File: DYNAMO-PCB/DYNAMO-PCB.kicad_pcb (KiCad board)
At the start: 2 copper layers, 43 parts, among them J1 HDMI_A, J10 Conn_01x03_Pin, J11 Conn_01x03_Pin, J12 Conn_01x03_Pin, J13 Conn_01x02_Pin, J17 USB3_A, J18 USB3_A, J19 USB3_A, J2 USB3_A, J20 USB3_A, J21 USB3_A, J22 USB3_A, J23 USB3_A, J24 USB3_A, J25 USB3_A, J26 USB_C_Receptacle_USB2.0_16P, J27 USB_C_Receptacle_USB2.0_16P, J28 USB_C_Receptacle_USB2.0_16P, J29 USB_C_Receptacle_USB2.0_16P, J3 Conn_01x03_Pin, J30 USB_C_Receptacle_USB2.0_16P, J31 USB3_A, J32 USB3_A, J33 Conn_02x05_Counter_Clockwise, J34 Conn_02x05_Counter_Clockwise, J5 Conn_01x02_Pin, J6 Conn_01x03_Pin, J7 Conn_01x08_Socket, J8 Conn_01x03_Pin, J9 Conn_01x03_Pin, U2 CH7035B-BF

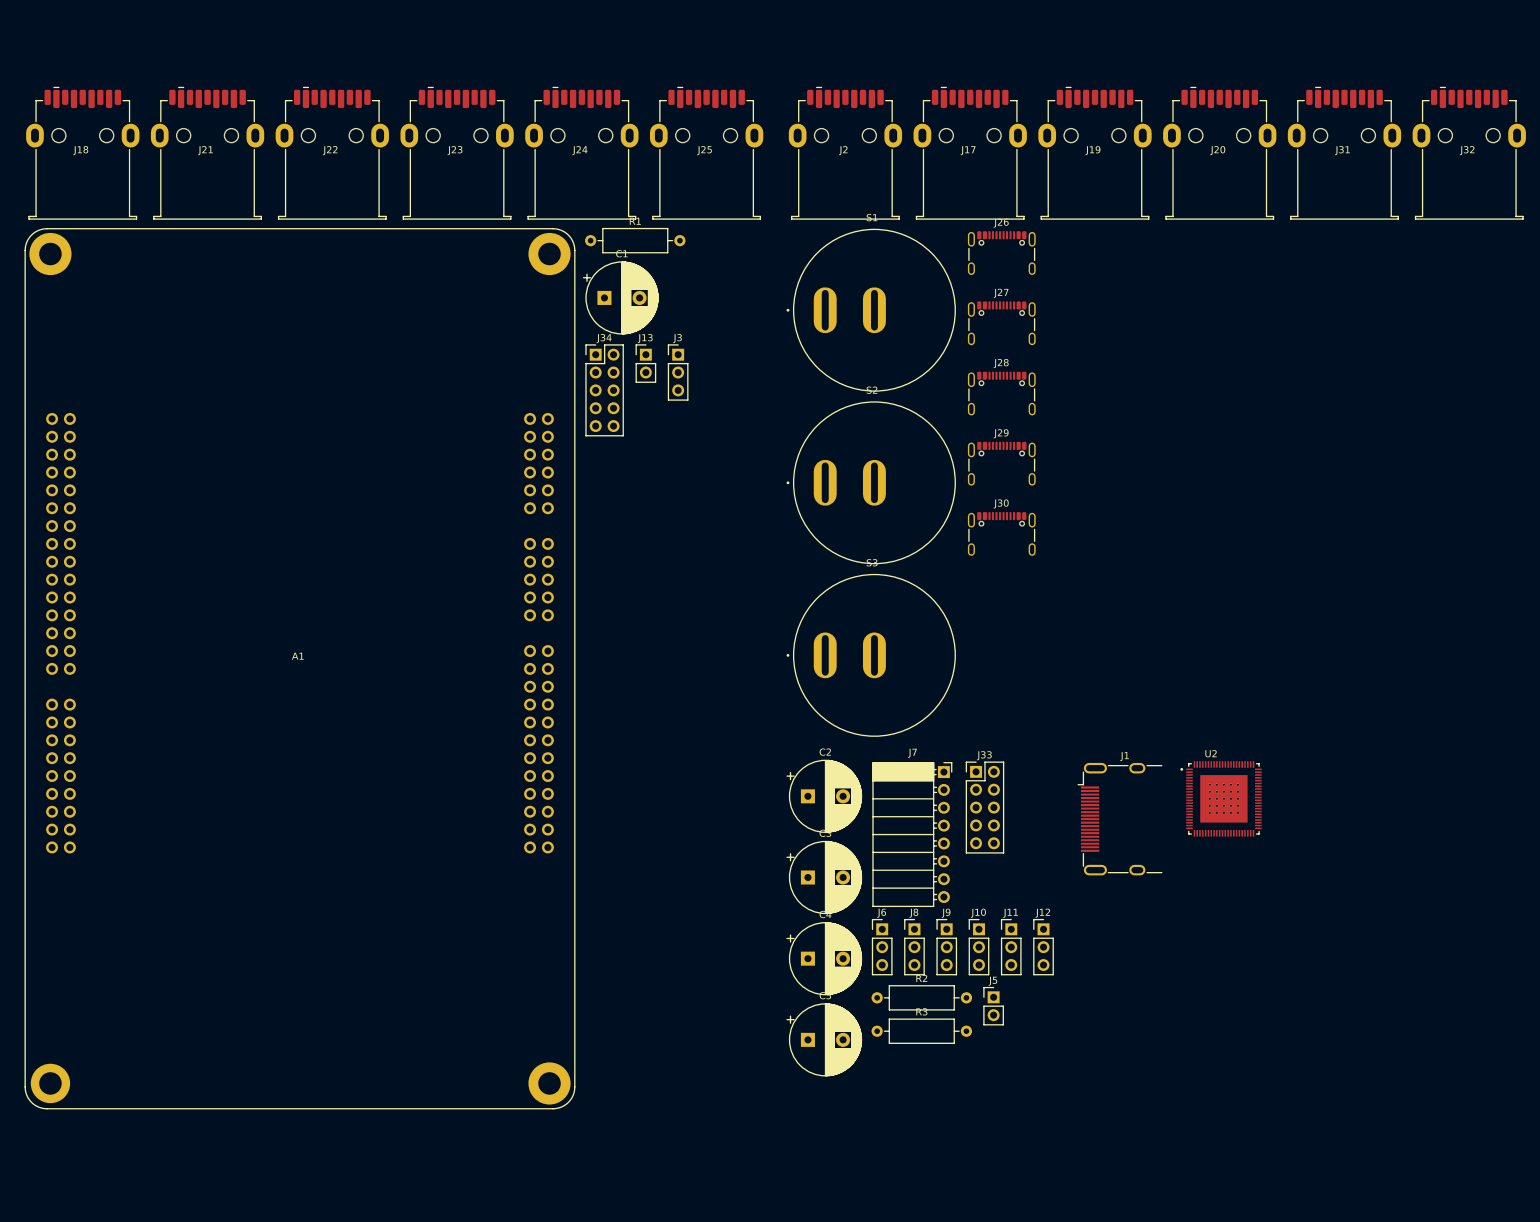
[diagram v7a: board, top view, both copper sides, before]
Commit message: schematic complete (pre-ERC)
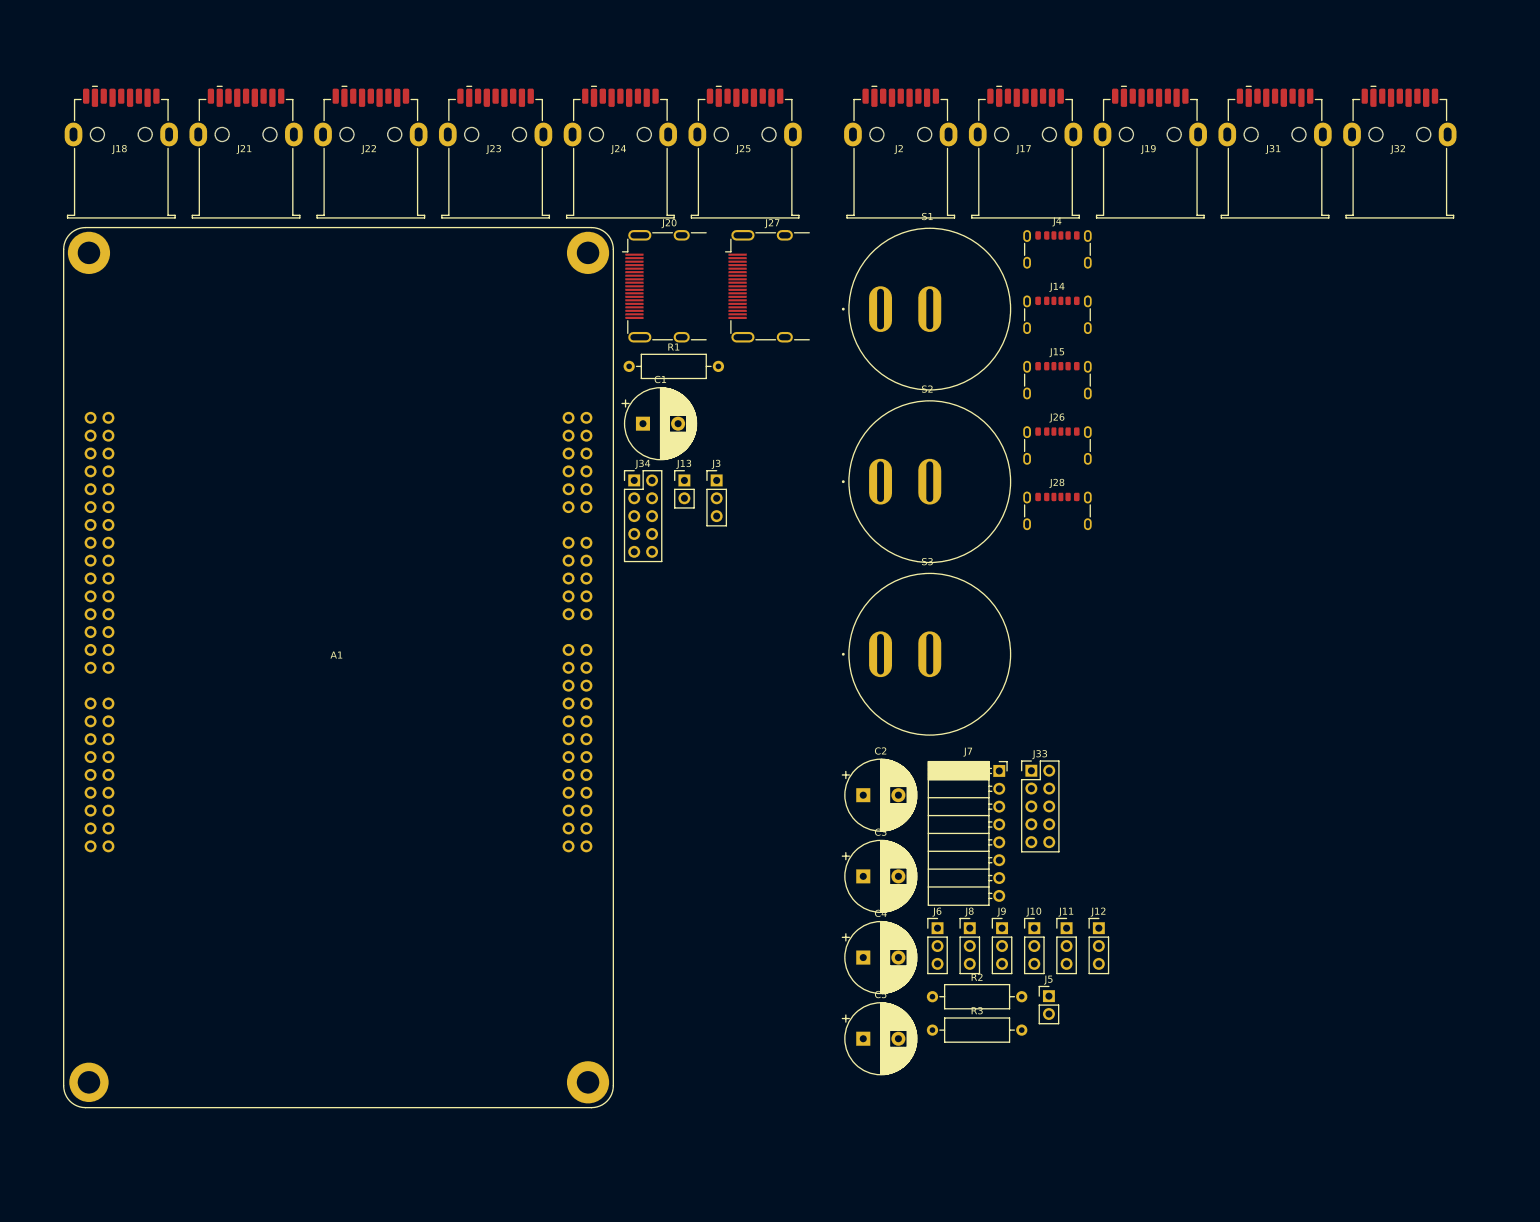
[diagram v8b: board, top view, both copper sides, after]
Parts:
- removed J1: HDMI_A, Connector_Video:HDMI_A_Molex_208658-1001_Horizontal
- removed J29, J30: USB_C_Receptacle_USB2.0_16P, Connector_USB:USB_C_Receptacle_GCT_USB4105-xx-A_16P_TopMnt_Horizontal
- removed U2: CH7035B-BF, CH7035B-BF:QFN40P1000X1000X90-89N
- added J14: USB_C_Receptacle_PowerOnly_6P, Connector_USB:USB_C_Receptacle_GCT_USB4125-xx-x_6P_TopMnt_Horizontal, F.Cu at (192.9, 58.2)
- added J15: USB_C_Receptacle_PowerOnly_6P, Connector_USB:USB_C_Receptacle_GCT_USB4125-xx-x_6P_TopMnt_Horizontal, F.Cu at (192.9, 67.5)
- added J4: USB_C_Receptacle_PowerOnly_6P, Connector_USB:USB_C_Receptacle_GCT_USB4125-xx-x_6P_TopMnt_Horizontal, F.Cu at (192.9, 48.9)
- C1: value C_Polarized -> 1000µF
- C2, C3, C4, C5: value C_Polarized -> 470µF
- J20: value USB3_A -> HDMI_A; footprint 692122030100:692122030100 -> Connector_Video:HDMI_A_Molex_208658-1001_Horizontal
- J26, J28: value USB_C_Receptacle_USB2.0_16P -> USB_C_Receptacle_PowerOnly_6P; footprint Connector_USB:USB_C_Receptacle_GCT_USB4105-xx-A_16P_TopMnt_Horizontal -> Connector_USB:USB_C_Receptacle_GCT_USB4125-xx-x_6P_TopMnt_Horizontal
- J27: value USB_C_Receptacle_USB2.0_16P -> HDMI_A; footprint Connector_USB:USB_C_Receptacle_GCT_USB4105-xx-A_16P_TopMnt_Horizontal -> Connector_Video:HDMI_A_Molex_208658-1001_Horizontal
- R1, R2, R3: value R -> 330
- moved J20 82.0 mm to (136.0, 53.0)
- moved J27 34.9 mm to (150.7, 53.0)
- moved J26 28.5 mm to (192.9, 76.8)
- moved C1 18.7 mm to (133.9, 72.6)
- moved J3 18.7 mm to (144.4, 80.7)
- moved R1 18.7 mm to (131.9, 64.4)
- moved J13 18.7 mm to (139.8, 80.7)
- moved J34 18.7 mm to (132.7, 80.7)
- moved J28 18.4 mm to (192.9, 86.1)
- moved J31 9.88 mm to (223.6, 34.0)
- moved J32 9.88 mm to (241.4, 34.0)
- moved C2 7.87 mm to (165.3, 125.4)
- moved C3 7.87 mm to (165.3, 137.0)
- moved C4 7.87 mm to (165.3, 148.5)
- moved C5 7.87 mm to (165.3, 160.1)
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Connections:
- A1 pad 11: unconnected-(A1A-D6-Pad11) -> Net-(A1A-D6)
- A1 pad 12: unconnected-(A1A-D13-Pad12) -> Net-(A1A-D13)
- A1 pad 16: unconnected-(A1A-D11-Pad16) -> Net-(A1A-D11)
- A1 pad 17: unconnected-(A1A-D3/SCL-Pad17) -> Net-(A1A-D3/SCL)
- A1 pad 18: unconnected-(A1A-D10-Pad18) -> Net-(A1A-D10)
- A1 pad 19: unconnected-(A1A-D2/SDA-Pad19) -> Net-(A1A-D2/SDA)
- A1 pad 20: unconnected-(A1A-D9-Pad20) -> Net-(A1A-D9)
- A1 pad 22: unconnected-(A1A-D8-Pad22) -> Net-(A1A-D8)
- A1 pad 24: unconnected-(A1A-D7-Pad24) -> Net-(A1A-D7)
- C1 pad 1: unconnected-(C1-Pad1) -> /Power Distribution/+5V peripherals
- C1 pad 2: unconnected-(C1-Pad2) -> GND
- C2 pad 2: Net-(J10-Pin_3) -> GND
- C3 pad 2: Net-(J10-Pin_3) -> GND
- C4 pad 2: Net-(J10-Pin_3) -> GND
- C5 pad 2: Net-(J10-Pin_3) -> GND
- J10 pad 1: Net-(J10-Pin_1) -> GND
- J11 pad 1: Net-(J11-Pin_1) -> GND
- J11 pad 2: Net-(J10-Pin_2) -> Net-(J11-Pin_2)
- J11 pad 3: Net-(J10-Pin_3) -> Net-(J10-Pin_2)
- J12 pad 1: Net-(J12-Pin_1) -> Net-(J10-Pin_2)
- J12 pad 2: Net-(J10-Pin_2) -> Net-(J12-Pin_2)
- J12 pad 3: Net-(J10-Pin_3) -> Net-(J10-Pin_2)
- J13 pad 1: unconnected-(J13-Pin_1-Pad1) -> /Power Distribution/+5V peripherals
- J13 pad 2: unconnected-(J13-Pin_2-Pad2) -> GND
- J17 pad 1: Net-(J17-VBUS) -> /Power Distribution/+5V peripherals
- J17 pad 4: Net-(J17-GND) -> GND
- J18 pad 4: Net-(J18-GND) -> GND
- J19 pad 10: Net-(J19-SHIELD) -> Net-(J17-SHIELD)
- J19 pad 2: Net-(J19-D-) -> unconnected-(J19-D--Pad2)
- J19 pad 3: Net-(J19-D+) -> unconnected-(J19-D+-Pad3)
- J19 pad 4: Net-(J17-GND) -> GND
- J19 pad 5: Net-(J19-SSRX-) -> unconnected-(J19-SSRX--Pad5)
- J19 pad 6: Net-(J19-SSRX+) -> unconnected-(J19-SSRX+-Pad6)
- J19 pad 7: Net-(J19-DRAIN) -> unconnected-(J19-DRAIN-Pad7)
- J19 pad 8: Net-(J19-SSTX-) -> unconnected-(J19-SSTX--Pad8)
- J19 pad 9: Net-(J19-SSTX+) -> unconnected-(J19-SSTX+-Pad9)
- J2 pad 1: Net-(J17-VBUS) -> /Power Distribution/+5V peripherals
- J2 pad 4: Net-(J17-GND) -> GND
- J20 pad 1: Net-(J17-VBUS) -> Net-(J20-D2+)
- J20 pad 10: Net-(J19-SHIELD) -> Net-(J20-CK+)
- J20 pad 2: Net-(J19-D-) -> GND
- J20 pad 3: Net-(J19-D+) -> Net-(J20-D2-)
- J20 pad 4: Net-(J17-GND) -> Net-(J20-D1+)
- J20 pad 5: Net-(J19-SSRX-) -> GND
- J20 pad 6: Net-(J19-SSRX+) -> Net-(J20-D1-)
- J20 pad 7: Net-(J19-DRAIN) -> Net-(J20-D0+)
- J20 pad 8: Net-(J19-SSTX-) -> GND
- J20 pad 9: Net-(J19-SSTX+) -> Net-(J20-D0-)
- J21 pad 4: Net-(J21-GND) -> GND
- J22 pad 4: Net-(J22-GND) -> GND
- J23 pad 4: Net-(J18-GND) -> GND
- J24 pad 4: Net-(J22-GND) -> GND
- J25 pad 4: Net-(J21-GND) -> GND
- J26 pad A12: Net-(J26-GND-PadA1) -> GND
- J26 pad A9: Net-(J26-VBUS-PadA4) -> Net-(J26-VBUS-PadA9)
- J26 pad B12: Net-(J26-GND-PadA1) -> GND
- J26 pad B9: Net-(J26-VBUS-PadA4) -> Net-(J26-VBUS-PadA9)
- J28 pad A12: Net-(J26-GND-PadA1) -> GND
- J28 pad A9: Net-(J28-VBUS-PadA4) -> Net-(J28-VBUS-PadA9)
- J28 pad B12: Net-(J26-GND-PadA1) -> GND
- J28 pad B9: Net-(J28-VBUS-PadA4) -> Net-(J28-VBUS-PadA9)
- J3 pad 1: unconnected-(J3-Pin_1-Pad1) -> /Power Distribution/+5V peripherals
- J3 pad 2: unconnected-(J3-Pin_2-Pad2) -> Net-(J3-Pin_2)
- J3 pad 3: unconnected-(J3-Pin_3-Pad3) -> GND
- J31 pad 4: Net-(J31-GND) -> GND
- J32 pad 4: Net-(J31-GND) -> GND
- J33 pad 3: Net-(J10-Pin_1) -> Net-(J10-Pin_3)
- J33 pad 9: Net-(J10-Pin_3) -> GND
- J34 pad 1: unconnected-(J34-Pin_1-Pad1) -> Net-(A1A-D8)
- J34 pad 10: unconnected-(J34-Pin_10-Pad10) -> /Power Distribution/+5V peripherals
- J34 pad 2: unconnected-(J34-Pin_2-Pad2) -> Net-(A1A-D7)
- J34 pad 3: unconnected-(J34-Pin_3-Pad3) -> Net-(A1A-D9)
- J34 pad 4: unconnected-(J34-Pin_4-Pad4) -> Net-(A1A-D3/SCL)
- J34 pad 5: unconnected-(J34-Pin_5-Pad5) -> Net-(A1A-D2/SDA)
- J34 pad 6: unconnected-(J34-Pin_6-Pad6) -> Net-(A1A-D10)
- J34 pad 7: unconnected-(J34-Pin_7-Pad7) -> Net-(A1A-D11)
- J34 pad 8: unconnected-(J34-Pin_8-Pad8) -> Net-(A1A-D13)
- J34 pad 9: unconnected-(J34-Pin_9-Pad9) -> GND
- J5 pad 1: Net-(J10-Pin_2) -> GND
- J5 pad 2: Net-(J10-Pin_3) -> Net-(J10-Pin_2)
- J6 pad 1: Net-(J33-Pin_8) -> GND
- J6 pad 3: Net-(J10-Pin_3) -> Net-(J33-Pin_8)
- J7 pad 2: Net-(J10-Pin_3) -> GND
- J8 pad 1: Net-(J33-Pin_7) -> GND
- J8 pad 3: Net-(J10-Pin_3) -> Net-(J33-Pin_7)
- J9 pad 1: Net-(J33-Pin_6) -> GND
- J9 pad 3: Net-(J10-Pin_3) -> Net-(J33-Pin_6)
- R1 pad 1: unconnected-(R1-Pad1) -> Net-(A1A-D6)
- R1 pad 2: unconnected-(R1-Pad2) -> Net-(J3-Pin_2)
- R2 pad 2: Net-(J11-Pin_1) -> Net-(J11-Pin_2)
- R3 pad 2: Net-(J12-Pin_1) -> Net-(J12-Pin_2)
- S1 pad 1: Net-(J17-VBUS) -> /Power Distribution/+5V peripherals
- S2 pad 1: Net-(J28-VBUS-PadA4) -> Net-(J28-VBUS-PadA9)
- S2 pad 2: Net-(J26-VBUS-PadA4) -> Net-(J26-VBUS-PadA9)
